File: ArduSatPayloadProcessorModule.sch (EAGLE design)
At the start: 338 parts, among them IC1 ATMEGA328P QFN32, IC10 ATMEGA328P QFN32, IC11 ATMEGA328P QFN32, IC12 ATMEGA328P QFN32, IC13 ATMEGA328P QFN32, IC14 ATMEGA328P QFN32, IC15 ATMEGA328P QFN32, IC16 ATMEGA328P QFN32, IC17 TXB0104, IC18 TMP102, IC19 TMP102, IC2 ATMEGA328P QFN32, IC20 ATMEGA2561-16MU, IC21 MAX4372F, IC22 MAX4372F, IC23 MUX-74HC4067-QFNSMT, IC24 MUX-74HC4067-QFNSMT, IC3 ATMEGA328P QFN32, IC4 ATMEGA328P QFN32, IC5 ATMEGA328P QFN32, IC6 ATMEGA328P QFN32, IC7 ATMEGA328P QFN32, IC8 ATMEGA328P QFN32, IC9 ATMEGA328P QFN32, P1 microSD, Q1 RJU003N03 N-MOSFET, Q10 RJU003N03 N-MOSFET, Q11 RJU003N03 N-MOSFET, Q12 RJU003N03 N-MOSFET, Q13 RJU003N03 N-MOSFET, Q14 RJU003N03 N-MOSFET, Q15 RJU003N03 N-MOSFET, Q16 RJU003N03 N-MOSFET, Q17 RJU003N03 N-MOSFET, Q18 RJU003N03 N-MOSFET, Q19 RJU003N03 N-MOSFET, Q2 RJU003N03 N-MOSFET, Q20 RJU003N03 N-MOSFET, Q21 RJU003N03 N-MOSFET, Q22 RJU003N03 N-MOSFET, Q23 RJU003N03 N-MOSFET, Q24 RJU003N03 N-MOSFET, Q25 RJU003N03 N-MOSFET, Q26 RJU003N03 N-MOSFET, Q27 RJU003N03 N-MOSFET, Q28 RJU003N03 N-MOSFET, Q29 RJU003N03 N-MOSFET, Q3 RJU003N03 N-MOSFET, Q30 RJU003N03 N-MOSFET, Q31 RJU003N03 N-MOSFET, Q32 RJU003N03 N-MOSFET, Q33 RJU003N03 N-MOSFET, Q34 RJU003N03 N-MOSFET, Q35 RJU003N03 N-MOSFET, Q36 RJU003N03 N-MOSFET, Q37 RJU003N03 N-MOSFET, Q38 RJU003N03 N-MOSFET, Q39 RJU003N03 N-MOSFET, Q4 RJU003N03 N-MOSFET, Q40 RJU003N03 N-MOSFET, Q41 RJU003N03 N-MOSFET, Q42 RJU003N03 N-MOSFET, Q43 RJU003N03 N-MOSFET, Q44 RJU003N03 N-MOSFET, Q45 RJU003N03 N-MOSFET, Q46 RJU003N03 N-MOSFET, Q5 RJU003N03 N-MOSFET, Q6 RJU003N03 N-MOSFET, Q7 RJU003N03 N-MOSFET, Q8 RJU003N03 N-MOSFET, Q9 RJU003N03 N-MOSFET, SW1 ADG801 SOT23-6, SW10 ADG801 SOT23-6, SW11 ADG801 SOT23-6, SW12 ADG801 SOT23-6, SW13 ADG801 SOT23-6, SW14 ADG801 SOT23-6, SW15 ADG801 SOT23-6, SW16 ADG801 SOT23-6, SW17 RESET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

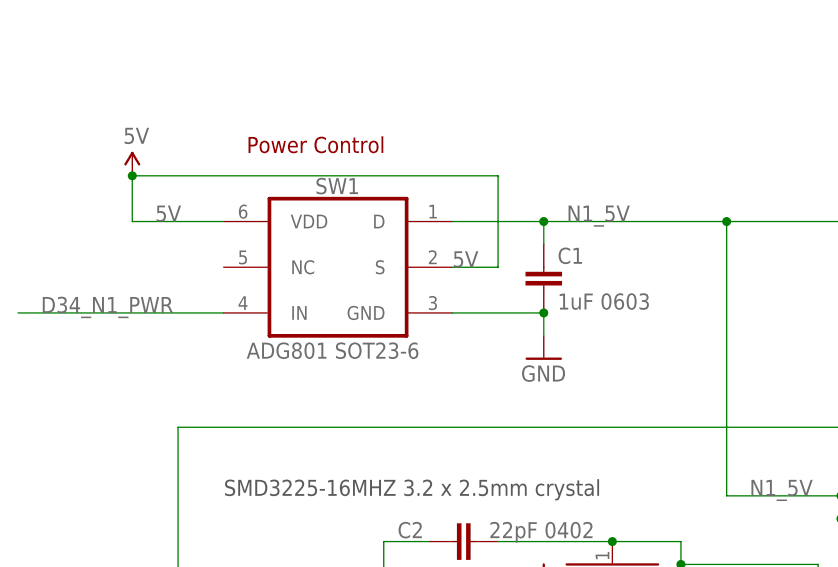
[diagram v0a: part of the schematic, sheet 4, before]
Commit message: Release 1.2: power jumpers on TMP102s; clearances
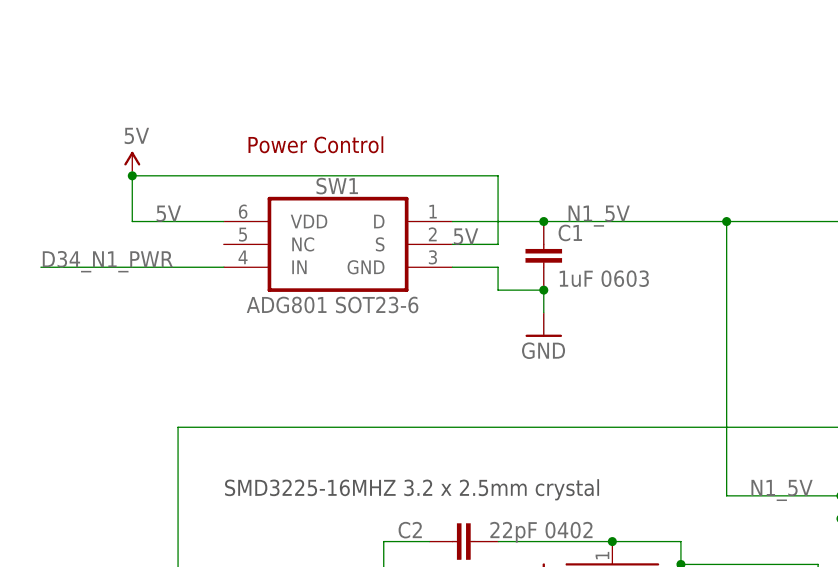
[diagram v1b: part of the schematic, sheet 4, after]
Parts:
- added SJ8, SJ9: SJC0402, freetronics-jon:SJC0402
- C59, C60: device freetronics:CAP_POL1206 -> freetronics-jon:CAP_POL1206
- LED17: value BLUE 0603 -> BLUE 0402
- P1: device freetronics-master-v1:USD-SOCKETNEW -> freetronics-master-v1.1:USD-SOCKETNEW
- renumbered U$26 to IC25
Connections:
- new net N$10010: IC18.V+, Q43.G, Q44.G, R83.2, R84.2, SJ8.2
- new net N$10011: IC19.ADD0, IC19.V+, Q45.G, Q46.G, R85.2, R86.2, SJ9.2
- net 3.3V: now also SJ8.1, SJ9.1; no longer IC18.V+, IC19.ADD0, IC19.V+, Q43.G, Q44.G, Q45.G, Q46.G, R83.2, R84.2, R85.2, R86.2
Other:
- note added: "V1.2 (2013-02-21)"
- note removed: "ATmega328P generates internal RESET pulse stretch"
- note removed: "Add watchdog (voltage + heartbeat?) to supervisor"
- note removed: "Bigger filter caps per node?"
- note removed: "GPS is susceptible to supply ripple. Extra decoupling or a filter to remove switching supply noise?"
- note removed: "V1.1 (2013-02-14)"
- moved on the sheet: C1, C12, C17, C20, C23, C26, C29, C32, C35, C38, C43, C46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
